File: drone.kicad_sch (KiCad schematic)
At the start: 0 parts

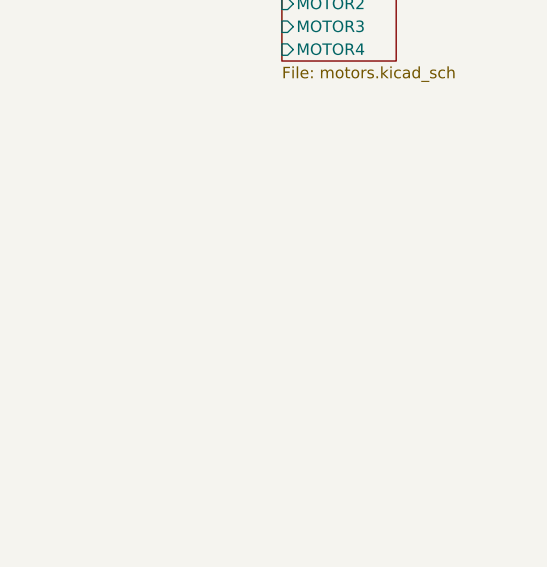
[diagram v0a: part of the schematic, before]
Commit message: Added FPGA power component
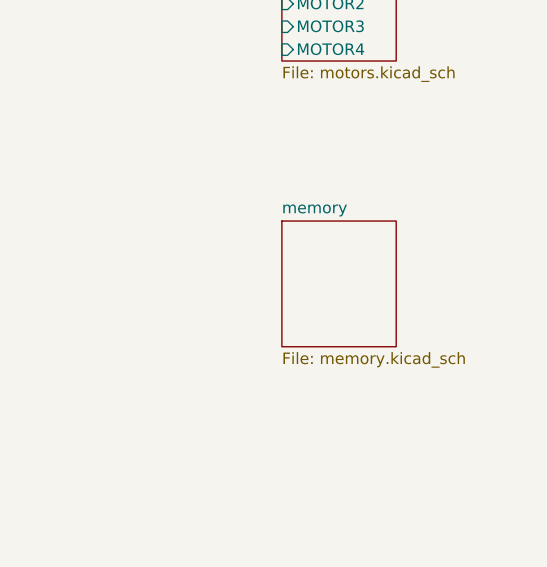
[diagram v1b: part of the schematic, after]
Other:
- added sheet memory (memory.kicad_sch)
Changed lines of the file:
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@@
+    )
+  )
+  (sheet (at 128.27 71.12) (size 12.7 13.97) (fields_autoplaced)
+    (stroke (width 0.1524) (type solid))
+    (fill (color 0 0 0 0.0000))
+    (property "Sheetname" "memory" (at 128.27 70.4084 0)
+      (effects (font (size 1.27 1.27)) (justify left bottom))
+    )
+    (property "Sheetfile" "memory.kicad_sch" (at 128.27 85.6746 0)
+      (effects (font (size 1.27 1.27)) (justify left top))
+    )
+    (instances
+      (project "drone"
+        (path "/d34d8324-c983-4098-8d7e-5c2fbd34794d" (page "7"))
+      )
     )
   )

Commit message: Prepare for power curcuit changes
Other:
- title: (none) -> Drone
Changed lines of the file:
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@@
 (kicad_sch (version 20230121) (generator eeschema)
   (paper "A5")
+  (title_block
+    (title "Drone")
+  )
   (sheet (at 128.27 43.18) (size 12.7 10.16) (fields_autoplaced)
     (stroke (width 0.1524) (type solid))

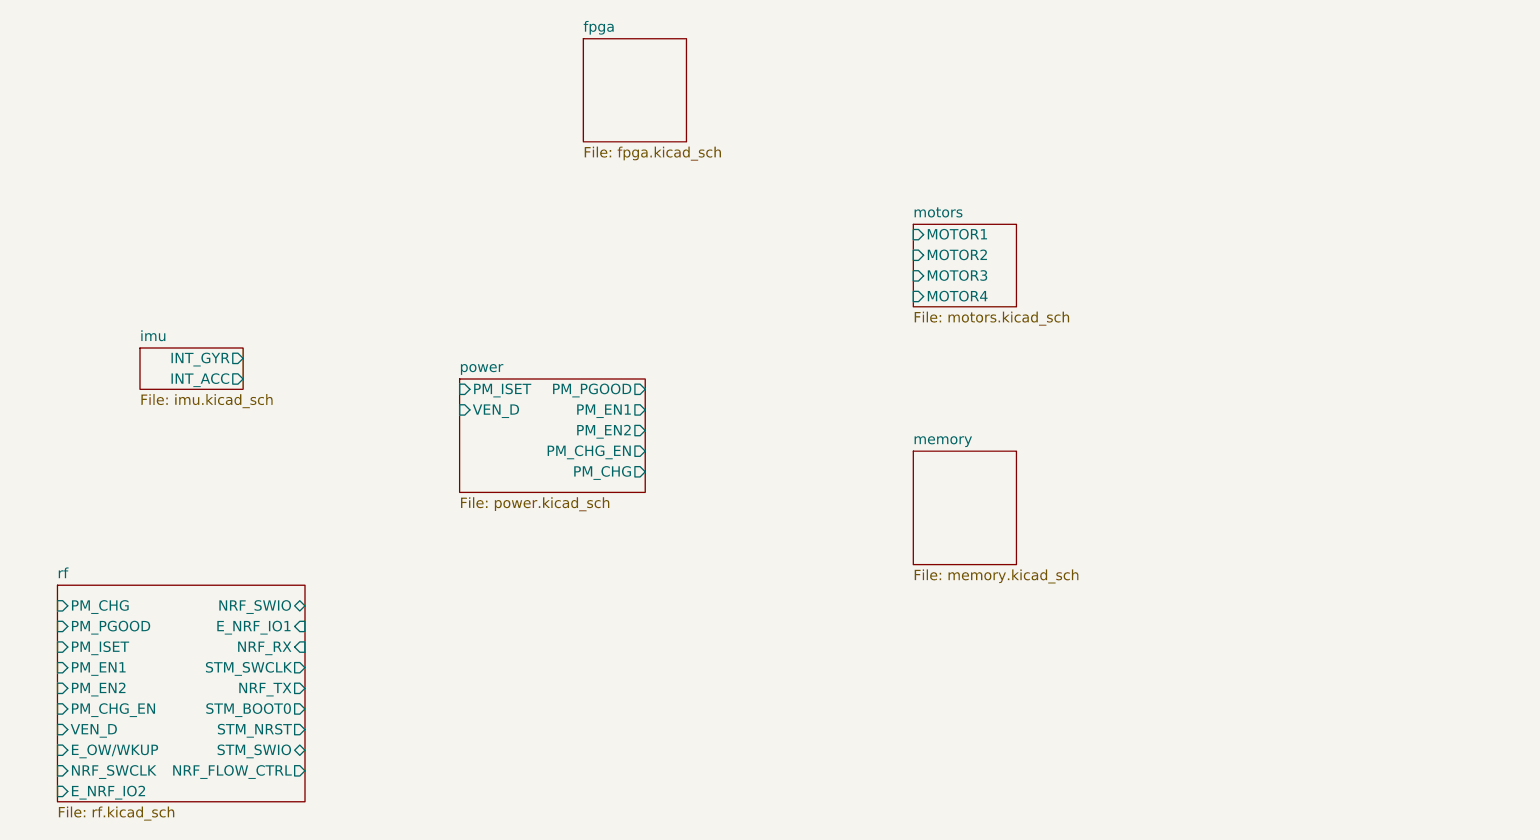
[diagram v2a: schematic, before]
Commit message: Moved USB-C connector to root sheet
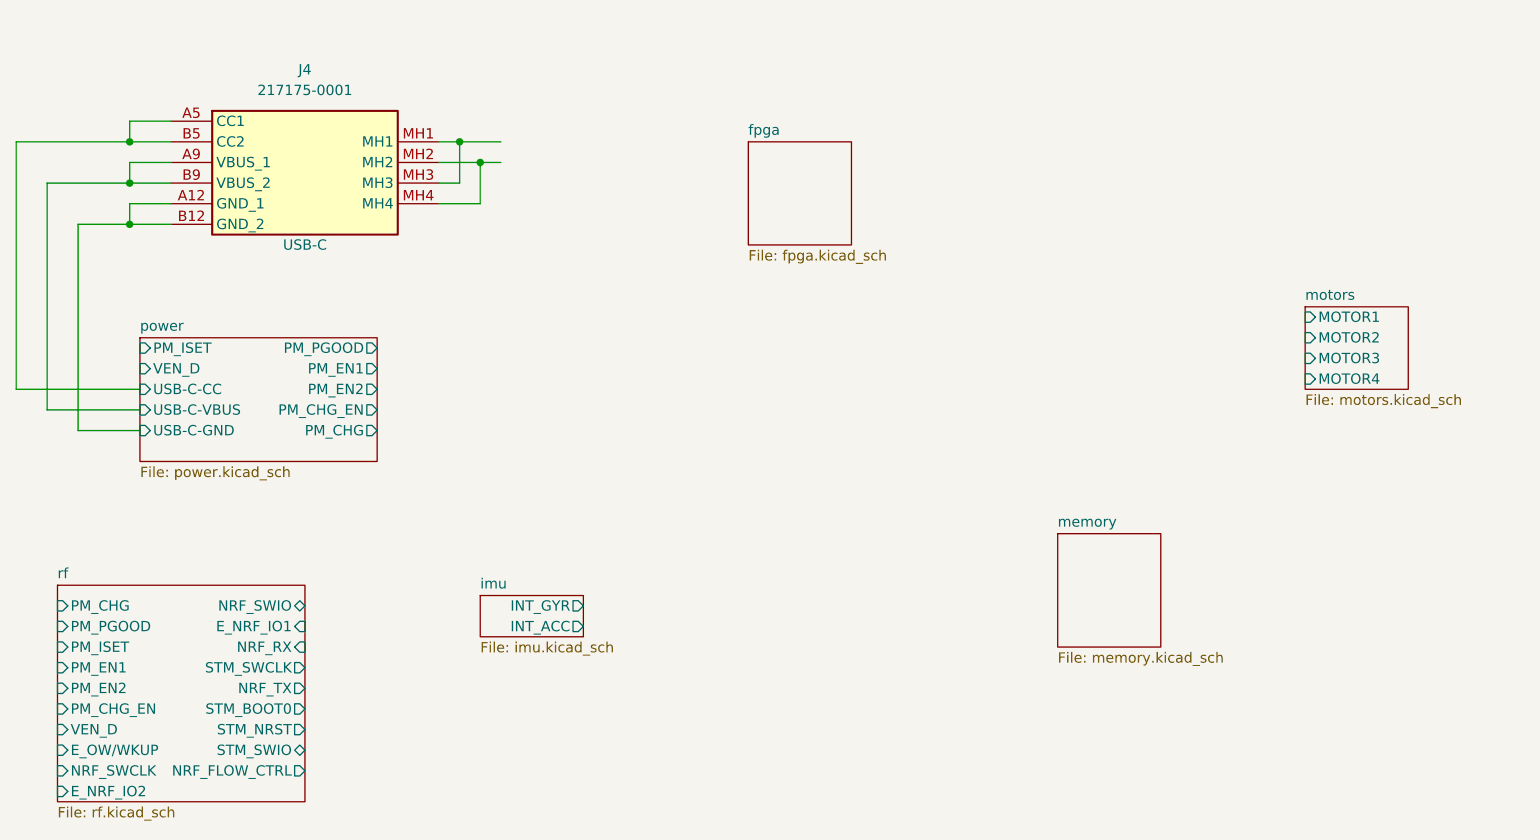
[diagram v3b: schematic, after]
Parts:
- added J4: 217175-0001, 2171750001, symbol SamacSys_Parts:217175-0001
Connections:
- new net: J4.MH1, J4.MH3
- new net: J4.MH2, J4.MH4
- new net power/USB-C-CC: J4.A5 (CC1), J4.B5 (CC2)
- new net power/USB-C-GND: J4.A12 (GND_1), J4.B12 (GND_2)
- new net power/USB-C-VBUS: J4.A9 (VBUS_1), J4.B9 (VBUS_2)
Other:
- sheet power ports: added USB-C-CC, USB-C-GND, USB-C-VBUS; removed none

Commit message: Removed RF module for now
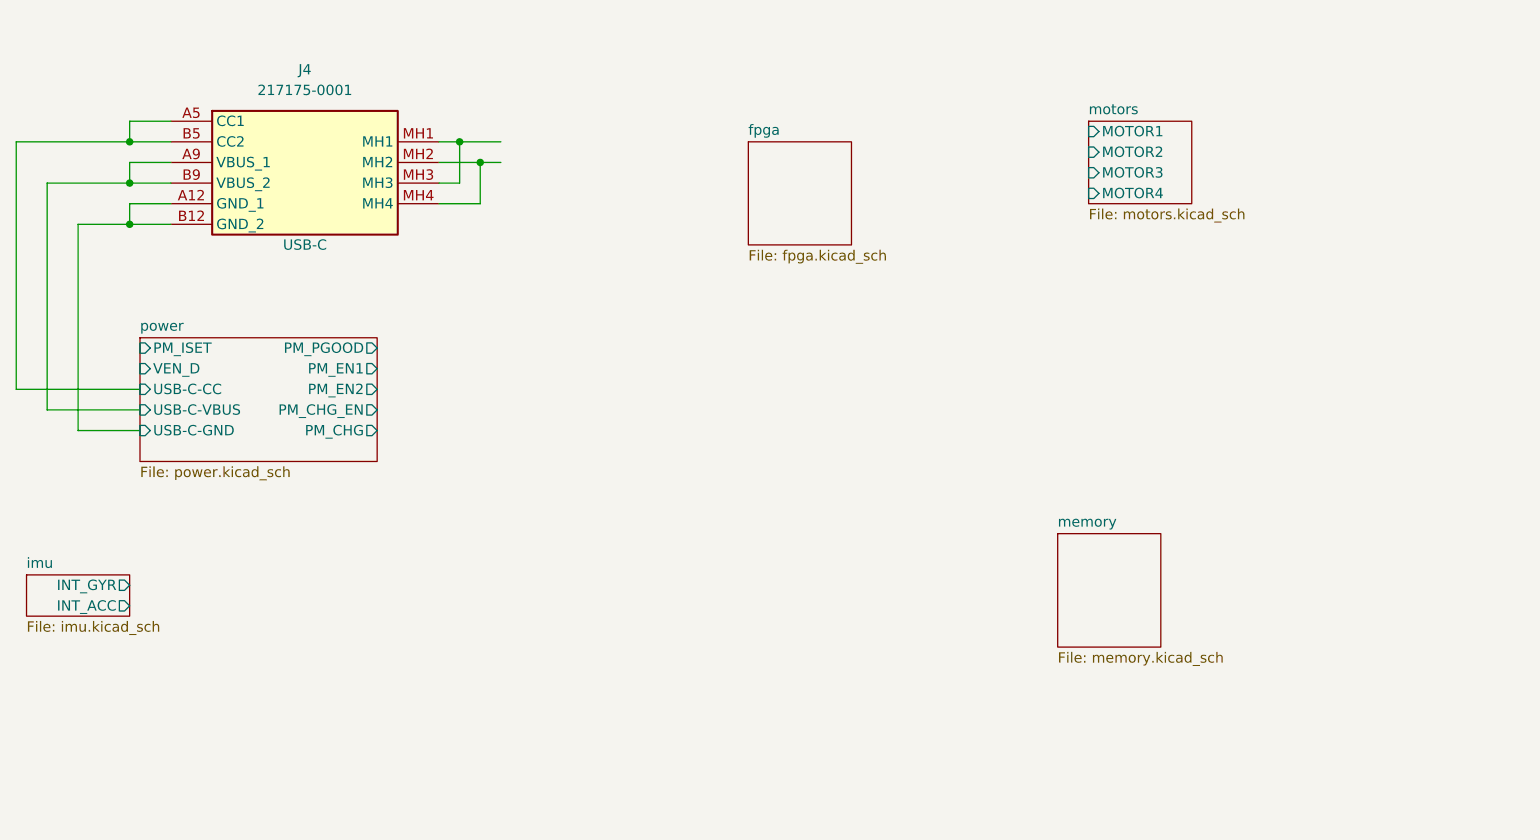
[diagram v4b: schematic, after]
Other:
- removed sheet rf
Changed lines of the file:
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@@
         )
         (path "/d34d8324-c983-4098-8d7e-5c2fbd34794d"
-          (reference "J2") (unit 1)
+          (reference "J1") (unit 1)
         )
       )
     )
   )
-  (sheet (at 176.53 53.34) (size 12.7 10.16) (fields_autoplaced)
+  (sheet (at 149.86 30.48) (size 12.7 10.16) (fields_autoplaced)
     (stroke (width 0.1524) (type solid))
     (fill (color 0 0 0 0.0000))
-    (property "Sheetname" "motors" (at 176.53 52.6284 0)
+    (property "Sheetname" "motors" (at 149.86 29.7684 0)
       (effects (font (size 1.27 1.27)) (justify left bottom))
     )
-    (property "Sheetfile" "motors.kicad_sch" (at 176.53 64.0846 0)
+    (property "Sheetfile" "motors.kicad_sch" (at 149.86 41.2246 0)
       (effects (font (size 1.27 1.27)) (justify left top))
     )
-    (pin "MOTOR3" input (at 176.53 59.69 180)
+    (pin "MOTOR3" input (at 149.86 36.83 180)
       (effects (font (size 1.27 1.27)) (justify left))
     )
-    (pin "MOTOR2" input (at 176.53 57.15 180)
+    (pin "MOTOR2" input (at 149.86 34.29 180)
       (effects (font (size 1.27 1.27)) (justify left))
     )
-    (pin "MOTOR1" input (at 176.53 54.61 180)
+    (pin "MOTOR1" input (at 149.86 31.75 180)
       (effects (font (size 1.27 1.27)) (justify left))
     )
-    (pin "MOTOR4" input (at 176.53 62.23 180)
+    (pin "MOTOR4" input (at 149.86 39.37 180)
       (effects (font (size 1.27 1.27)) (justify left))
     )
@@
     )
   )
-  (sheet (at 74.93 88.9) (size 12.7 5.08) (fields_autoplaced)
+  (sheet (at 19.05 86.36) (size 12.7 5.08) (fields_autoplaced)
     (stroke (width 0.1524) (type solid))
     (fill (color 0 0 0 0.0000))
-    (property "Sheetname" "imu" (at 74.93 88.1884 0)
+    (property "Sheetname" "imu" (at 19.05 85.6484 0)
       (effects (font (size 1.27 1.27)) (justify left bottom))
     )
-    (property "Sheetfile" "imu.kicad_sch" (at 74.93 94.5646 0)
+    (property "Sheetfile" "imu.kicad_sch" (at 19.05 92.0246 0)
       (effects (font (size 1.27 1.27)) (justify left top))
     )
-    (pin "INT_GYR" output (at 87.63 90.17 0)
+    (pin "INT_GYR" output (at 31.75 87.63 0)
       (effects (font (size 1.27 1.27)) (justify right))
     )
-    (pin "INT_ACC" output (at 87.63 92.71 0)
+    (pin "INT_ACC" output (at 31.75 90.17 0)
       (effects (font (size 1.27 1.27)) (justify right))
     )
@@
       )
     )
-  )
-  (sheet (at 22.86 87.63) (size 30.48 26.67) (fields_autoplaced)
-    (stroke (width 0.1524) (type solid))
-    (fill (color 0 0 0 0.0000))
-    (property "Sheetname" "rf" (at 22.86 86.9184 0)
-      (effects (font (size 1.27 1.27)) (justify left bottom))
-    )
-    (property "Sheetfile" "rf.kicad_sch" (at 22.86 114.8846 0)
-      (effects (font (size 1.27 1.27)) (justify left top))
-    )
-    (pin "PM_CHG" input (at 22.86 90.17 180)
-      (effects (font (size 1.27 1.27)) (justify left))
-    )
-    (pin "PM_PGOOD" input (at 22.86 92.71 180)
-      (effects (font (size 1.27 1.27)) (justify left))
-    )
-    (pin "PM_ISET" input (at 22.86 95.25 180)
-      (effects (font (size 1.27 1.27)) (justify left))
-    )
-    (pin "PM_EN1" input (at 22.86 97.79 180)
-      (effects (font (size 1.27 1.27)) (justify left))
-    )
-    (pin "PM_EN2" input (at 22.86 100.33 180)
-      (effects (font (size 1.27 1.27)) (justify left))
-    )
-    (pin "PM_CHG_EN" input (at 22.86 102.87 180)
-      (effects (font (size 1.27 1.27)) (justify left))
-    )
-    (pin "VEN_D" input (at 22.86 105.41 180)
-      (effects (font (size 1.27 1.27)) (justify left))
-    )
-    (pin "E_OW{slash}WKUP" input (at 22.86 107.95 180)
-      (effects (font (size 1.27 1.27)) (justify left))
-    )
-    (pin "NRF_SWCLK" input (at 22.86 110.49 180)
-      (effects (font (size 1.27 1.27)) (justify left))
-    )
-    (pin "E_NRF_IO2" input (at 22.86 113.03 180)
-      (effects (font (size 1.27 1.27)) (justify left))
-    )
-    (pin "NRF_FLOW_CTRL" output (at 53.34 110.49 0)
-      (effects (font (size 1.27 1.27)) (justify right))
-    )
-    (pin "NRF_SWIO" tri_state (at 53.34 90.17 0)
-      (effects (font (size 1.27 1.27)) (justify right))
-    )
-    (pin "E_NRF_IO1" input (at 53.34 92.71 0)
-      (effects (font (size 1.27 1.27)) (justify right))
-    )
-    (pin "NRF_RX" input (at 53.34 95.25 0)
-      (effects (font (size 1.27 1.27)) (justify right))
-    )
-    (pin "STM_SWCLK" output (at 53.34 97.79 0)
-      (effects (font (size 1.27 1.27)) (justify right))
-    )
-    (pin "NRF_TX" output (at 53.34 100.33 0)
-      (effects (font (size 1.27 1.27)) (justify right))
-    )
-    (pin "STM_BOOT0" output (at 53.34 102.87 0)
-      (effects (font (size 1.27 1.27)) (justify right))
-    )
-    (pin "STM_NRST" output (at 53.34 105.41 0)
-      (effects (font (size 1.27 1.27)) (justify right))
-    )
-    (pin "STM_SWIO" tri_state (at 53.34 107.95 0)
-      (effects (font (size 1.27 1.27)) (justify right))
-    )
-    (instances
-      (project "drone"
-        (path "/d34d8324-c983-4098-8d7e-5c2fbd34794d" (page "4"))
-      )
-    )

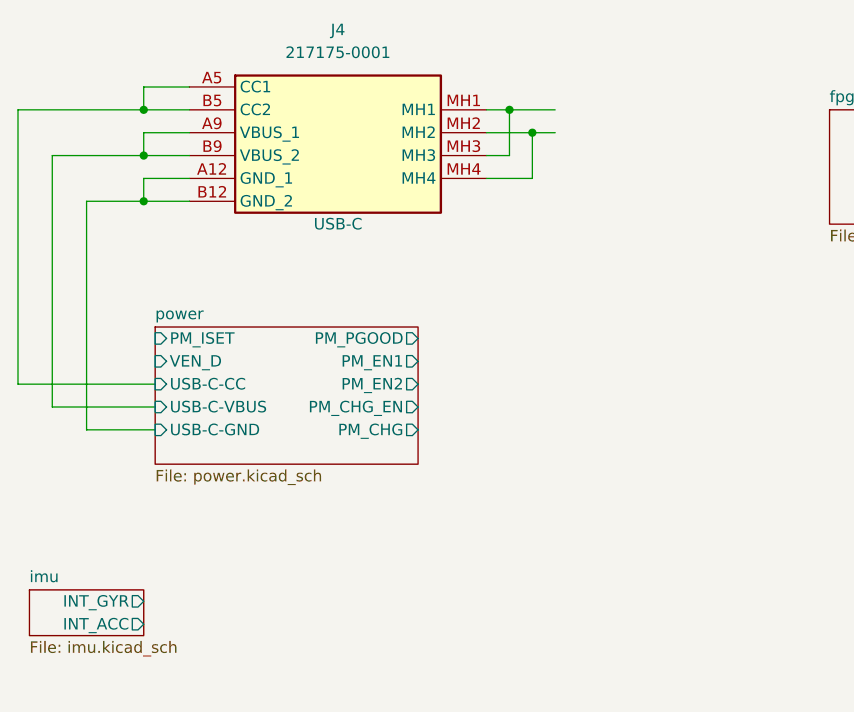
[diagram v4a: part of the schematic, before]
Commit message: Rewired power module
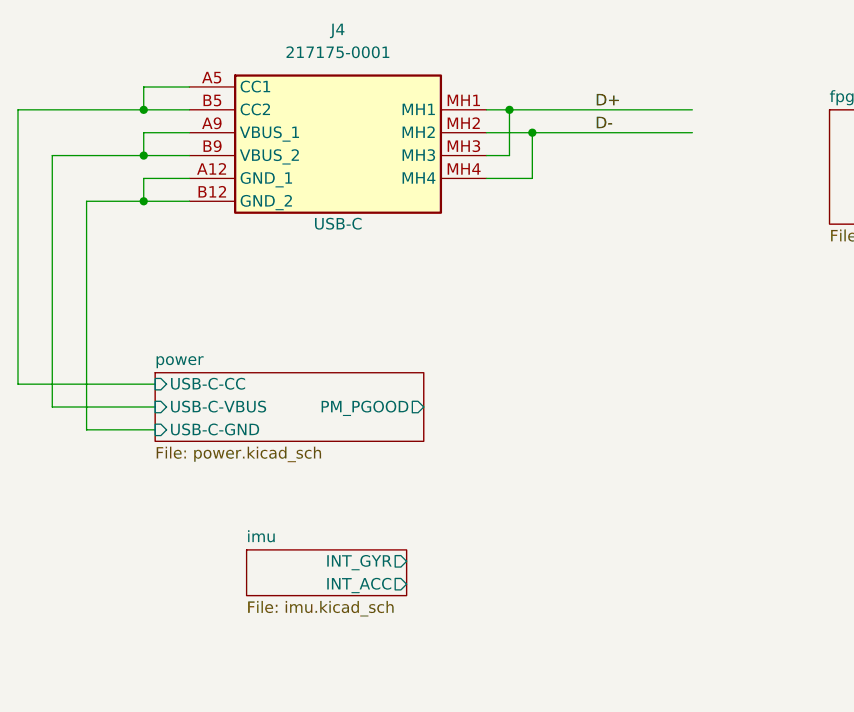
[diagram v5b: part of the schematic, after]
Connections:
- net D+: now reaches J4.MH1, J4.MH3
- net D-: now reaches J4.MH2, J4.MH4
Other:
- sheet power ports: added none; removed PM_CHG, PM_CHG_EN, PM_EN1, PM_EN2, PM_ISET, VEN_D
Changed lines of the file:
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@@
-    (stroke (width 0) (type default))
-  )
-  (wire (pts (xy 74.93 35.56) (xy 77.47 35.56))
     (stroke (width 0) (type default))
   )
@@
     (stroke (width 0) (type default))
   )
-  (wire (pts (xy 72.39 33.02) (xy 77.47 33.02))
+  (wire (pts (xy 72.39 33.02) (xy 92.71 33.02))
     (stroke (width 0) (type default))
   )
@@
   (wire (pts (xy 36.83 35.56) (xy 31.75 35.56))
     (stroke (width 0) (type default))
+  )
+  (wire (pts (xy 74.93 35.56) (xy 92.71 35.56))
+    (stroke (width 0) (type default))
+  )
+  (label "D-" (at 81.915 35.56 0) (fields_autoplaced)
+    (effects (font (size 1.27 1.27)) (justify left bottom))
+  )
+  (label "D+" (at 81.915 33.02 0) (fields_autoplaced)
+    (effects (font (size 1.27 1.27)) (justify left bottom))
   )
   (symbol (lib_id "SamacSys_Parts:217175-0001") (at 36.83 31.75 0) (unit 1)
@@
     (instances
       (project "drone"
-        (path "/d34d8324-c983-4098-8d7e-5c2fbd34794d" (page "7"))
+        (path "/d34d8324-c983-4098-8d7e-5c2fbd34794d" (page "6"))
       )
     )
@@
     (instances
       (project "drone"
-        (path "/d34d8324-c983-4098-8d7e-5c2fbd34794d" (page "6"))
-      )
-    )
-  )
-  (sheet (at 19.05 86.36) (size 12.7 5.08) (fields_autoplaced)
-    (stroke (width 0.1524) (type solid))
-    (fill (color 0 0 0 0.0000))
-    (property "Sheetname" "imu" (at 19.05 85.6484 0)
-      (effects (font (size 1.27 1.27)) (justify left bottom))
-    )
-    (property "Sheetfile" "imu.kicad_sch" (at 19.05 92.0246 0)
-      (effects (font (size 1.27 1.27)) (justify left top))
-    )
-    (pin "INT_GYR" output (at 31.75 87.63 0)
+        (path "/d34d8324-c983-4098-8d7e-5c2fbd34794d" (page "5"))
+      )
+    )
+  )
+  (sheet (at 43.18 81.915) (size 17.78 5.08) (fields_autoplaced)
+    (stroke (width 0.1524) (type solid))
+    (fill (color 0 0 0 0.0000))
+    (property "Sheetname" "imu" (at 43.18 81.2034 0)
+      (effects (font (size 1.27 1.27)) (justify left bottom))
+    )
+    (property "Sheetfile" "imu.kicad_sch" (at 43.18 87.5796 0)
+      (effects (font (size 1.27 1.27)) (justify left top))
+    )
+    (pin "INT_GYR" output (at 60.96 83.185 0)
       (effects (font (size 1.27 1.27)) (justify right))
     )
-    (pin "INT_ACC" output (at 31.75 90.17 0)
+    (pin "INT_ACC" output (at 60.96 85.725 0)
       (effects (font (size 1.27 1.27)) (justify right))
     )
@@
     )
   )
-  (sheet (at 33.02 57.15) (size 29.21 15.24) (fields_autoplaced)
-    (stroke (width 0.1524) (type solid))
-    (fill (color 0 0 0 0.0000))
-    (property "Sheetname" "power" (at 33.02 56.4384 0)
-      (effects (font (size 1.27 1.27)) (justify left bottom))
-    )
-    (property "Sheetfile" "power.kicad_sch" (at 33.02 72.9746 0)
-      (effects (font (size 1.27 1.27)) (justify left top))
-    )
-    (pin "PM_EN1" output (at 62.23 60.96 0)
+  (sheet (at 33.02 62.23) (size 29.845 7.62) (fields_autoplaced)
+    (stroke (width 0.1524) (type solid))
+    (fill (color 0 0 0 0.0000))
+    (property "Sheetname" "power" (at 33.02 61.5184 0)
+      (effects (font (size 1.27 1.27)) (justify left bottom))
+    )
+    (property "Sheetfile" "power.kicad_sch" (at 33.02 70.4346 0)
+      (effects (font (size 1.27 1.27)) (justify left top))
+    )
+    (pin "PM_PGOOD" output (at 62.865 66.04 0)
       (effects (font (size 1.27 1.27)) (justify right))
     )
-    (pin "PM_CHG_EN" output (at 62.23 66.04 0)
-      (effects (font (size 1.27 1.27)) (justify right))
-    )
-    (pin "PM_EN2" output (at 62.23 63.5 0)
-      (effects (font (size 1.27 1.27)) (justify right))
-    )
-    (pin "PM_CHG" output (at 62.23 68.58 0)
-      (effects (font (size 1.27 1.27)) (justify right))
-    )
-    (pin "PM_PGOOD" output (at 62.23 58.42 0)
-      (effects (font (size 1.27 1.27)) (justify right))
-    )
-    (pin "PM_ISET" input (at 33.02 58.42 180)
-      (effects (font (size 1.27 1.27)) (justify left))
-    )
-    (pin "VEN_D" input (at 33.02 60.96 180)
-      (effects (font (size 1.27 1.27)) (justify left))
-    )
     (pin "USB-C-CC" input (at 33.02 63.5 180)
       (effects (font (size 1.27 1.27)) (justify left))
@@
     (instances
       (project "drone"
-        (path "/d34d8324-c983-4098-8d7e-5c2fbd34794d" (page "5"))
-      )
-    )
+        (path "/d34d8324-c983-4098-8d7e-5c2fbd34794d" (page "4"))
+      )
+    )
